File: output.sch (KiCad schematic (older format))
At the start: 18 parts, among them U51 TXS0101DBV, U56 74LVC1G04

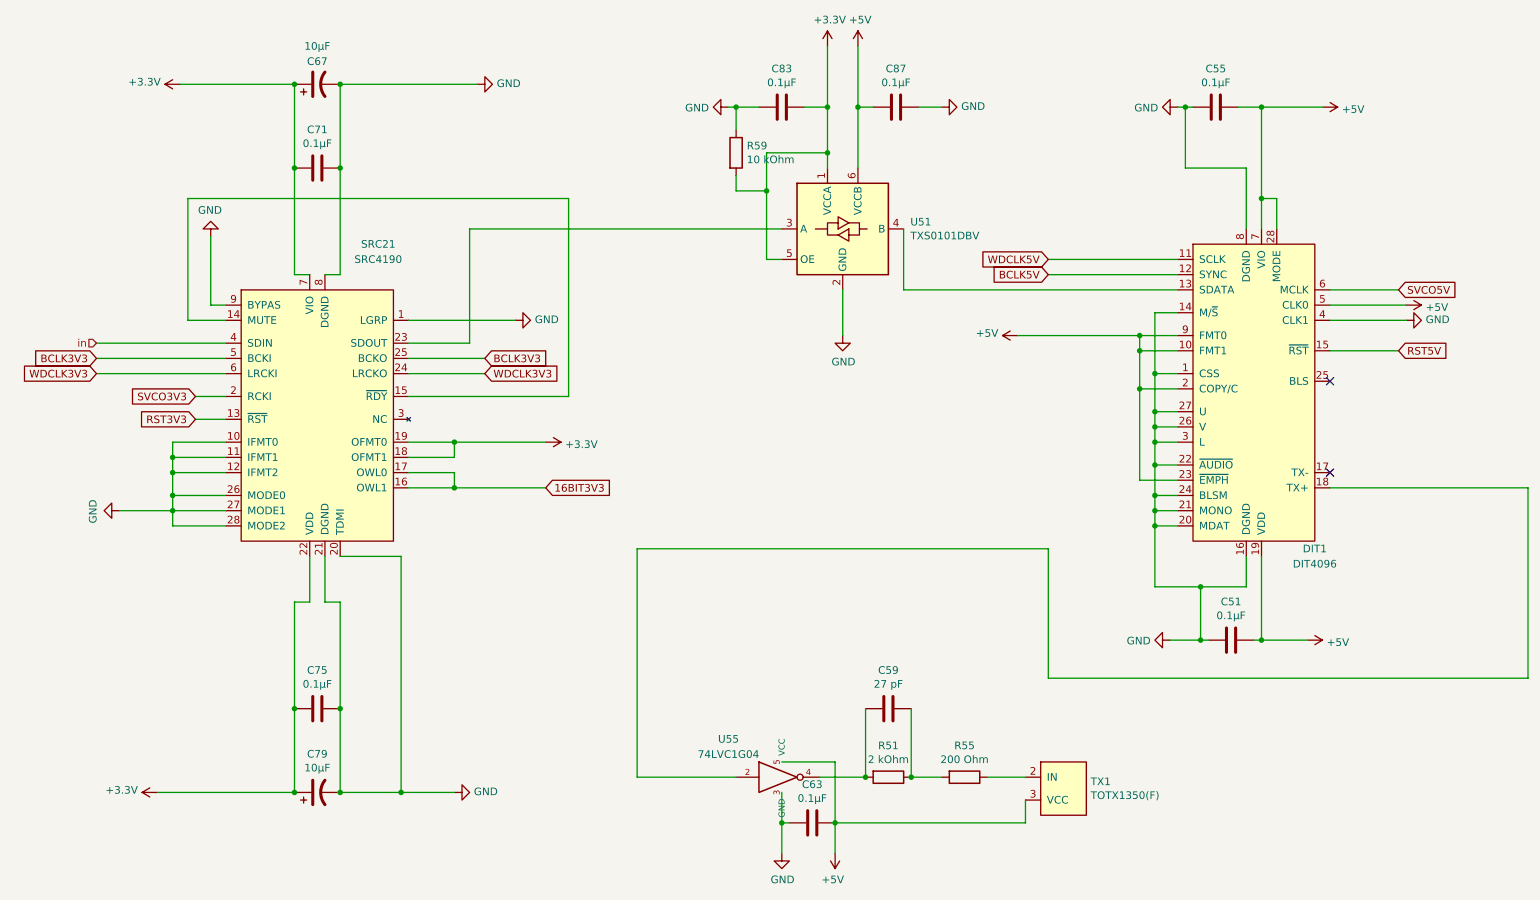
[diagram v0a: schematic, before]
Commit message: Remove dependency on digikey libraries.
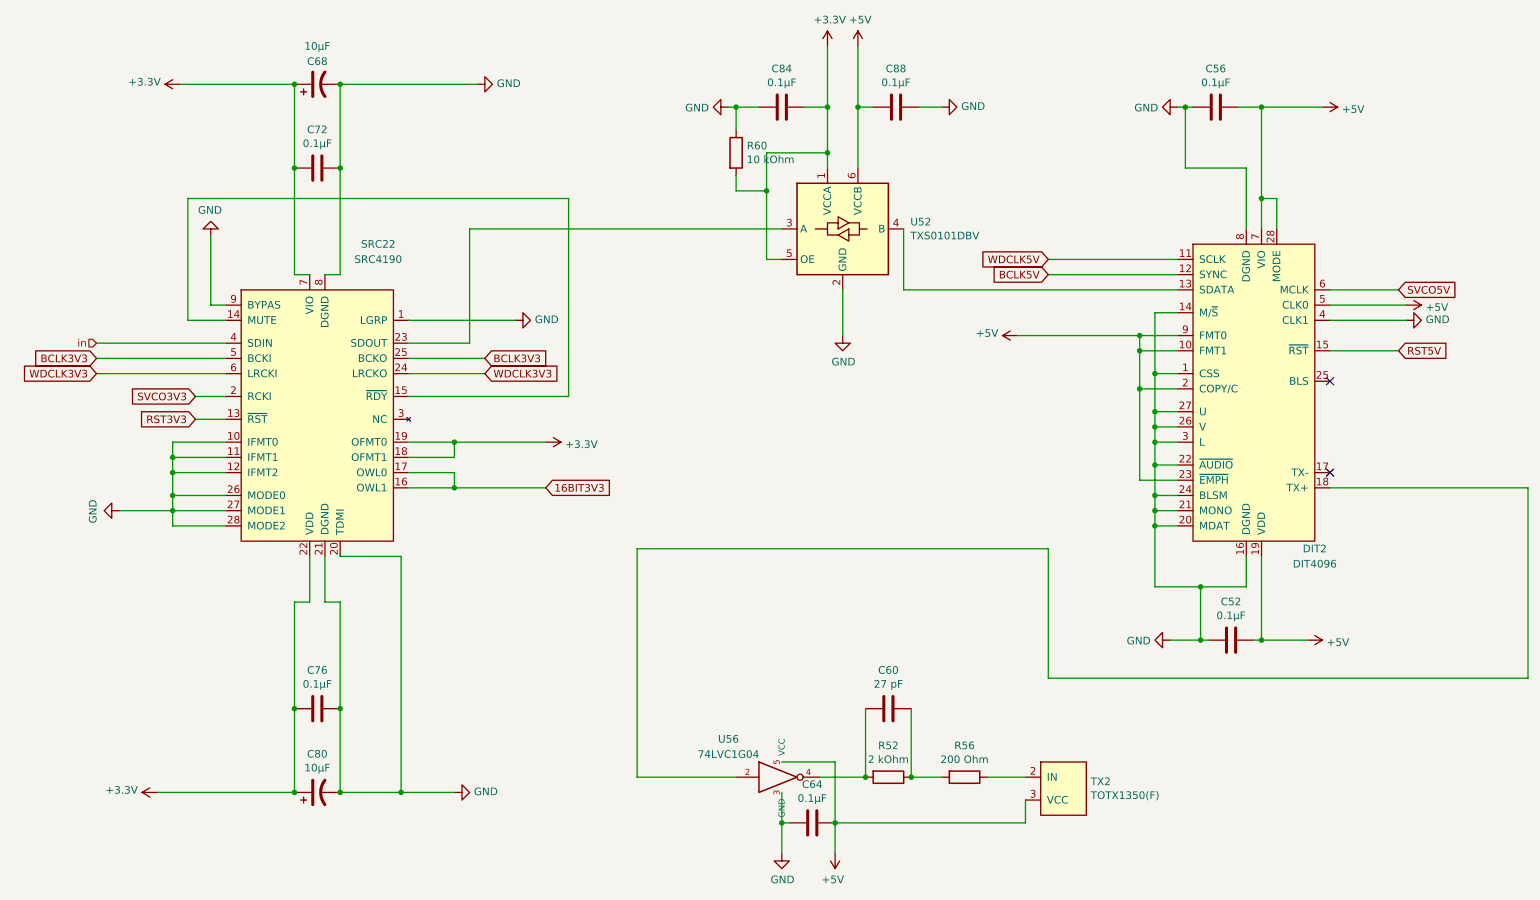
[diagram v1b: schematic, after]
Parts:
- DIT1: footprint digikey-footprints:TSSOP-28_W4.40mm -> Package_SO:TSSOP-28_4.4x9.7mm_P0.65mm
- SRC21: footprint digikey-footprints:SSOP-28_W5.30mm -> Package_SO:SSOP-28_5.3x10.2mm_P0.65mm
